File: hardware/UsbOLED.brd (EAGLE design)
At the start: 12.2 x 41.6 mm, 23 parts, among them U1 ATMEGA328P-MU-QFN32, X1 USBPCB

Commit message: urther refine
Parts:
- removed JP1: (no value), adafruit:1X06
- added H1: 1X6, headers(.1in):1X6
- R1: value 560kΩ -> 330kΩ
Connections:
- removed net N$10: C6.2, LCD1.5
- net +3V3: now also C6.2, H1.5, LCD1.5; no longer JP1.5
- net GND: now also H1.6; no longer JP1.6
- net MISO: now also H1.2; no longer JP1.2
- net MOSI: now also H1.1; no longer JP1.1
- net RST: now also H1.4; no longer JP1.4
- net SCK: now also H1.3; no longer JP1.3
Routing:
- net +3V3: track 61.4 -> 86.6 mm, vias 2 -> 4
- net N$10: track 18.2 -> 0.00 mm, vias 2 -> 0

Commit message: Improve routing, add version
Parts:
- removed C4: 10uF, rcl:C0603
- removed C6, C7: 1uF, rcl:C0603
- removed D3: (no value), diode:SOD523
- moved LOGO1 32.1 mm to (6.22, 4.57), flipped to the bottom
- moved D1 0.28 mm to (0.51, 11.2)
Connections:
- removed net N$11: C4.2, LCD1.14
- removed net N$9: C7.2, LCD1.8
- new net VCC: LCD1.14
- net +3V3: now also LCD1.8; no longer C6.2
- net +5V: no longer D3.C
- net GND: no longer C4.1, C6.1, C7.1
- net OLED_RESET: no longer D3.A
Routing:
- net D+: track 37.4 -> 18.2 mm
- net +5V: track 25.4 -> 9.63 mm, vias 2 -> 1
- net +3V3: track 86.6 -> 71.3 mm, vias 4 -> 5
- net SCK: track 14.1 -> 26.4 mm
- net N$9: track 9.04 -> 0.00 mm
- net OLED_RESET: track 15.5 -> 23.4 mm, vias 2 -> 0
- net GND: track 96.6 -> 92.1 mm
- net N$11: track 4.32 -> 0.00 mm
- net N$3: track 6.91 -> 10.5 mm, vias 0 -> 2
- net SDA: track 23.5 -> 26.4 mm, vias 3 -> 5
- net N$1: track 6.02 -> 8.57 mm, vias 0 -> 2
- net MISO: track 18.7 -> 21.2 mm
- net RST: track 12.2 -> 11.2 mm
- net D-: track 11.6 -> 12.1 mm
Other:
- board text added: "08.2018"
- board text added: "Mihai Galos"
- board text added: "UsbOLED v1.0.0"

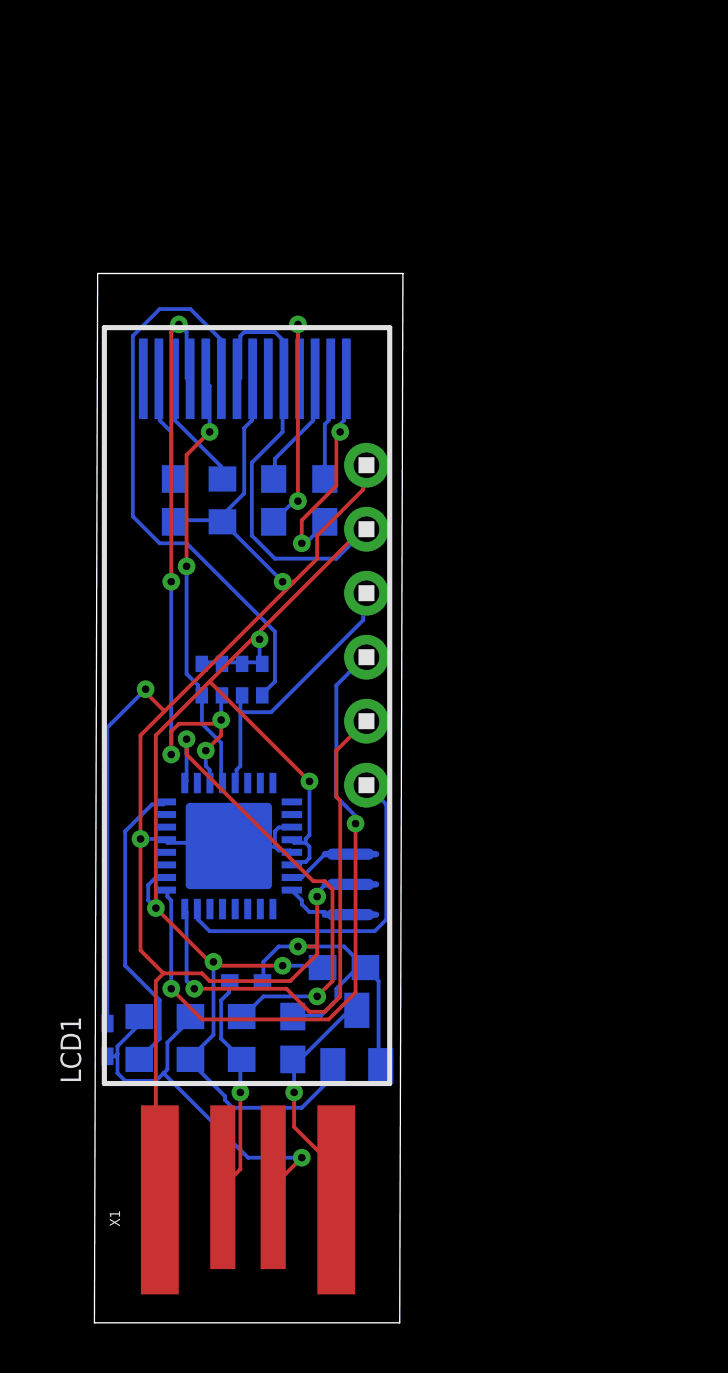
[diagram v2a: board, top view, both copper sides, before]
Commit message: Add pushbuttons A,B
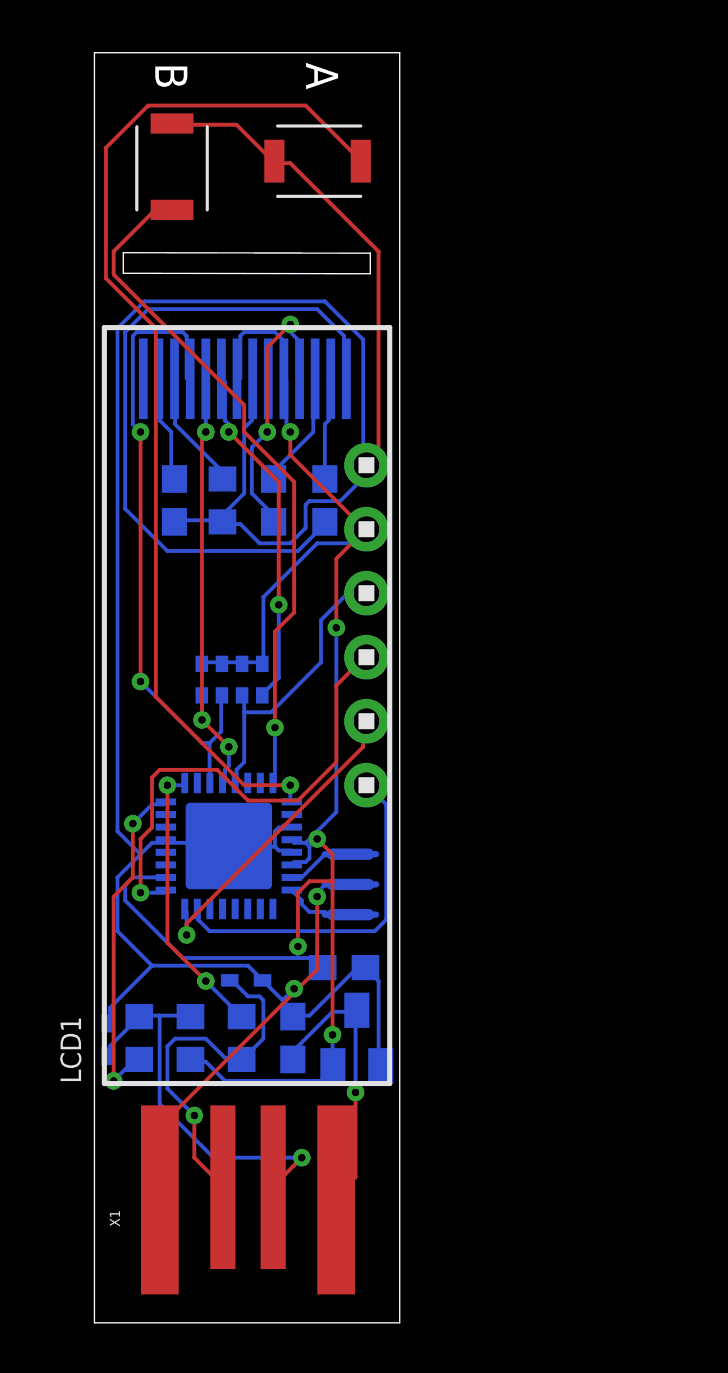
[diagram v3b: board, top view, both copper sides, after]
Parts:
- added U$1, U$3: PUSHBUTTON_4X2.5, pusbbutton_4x2_5:PUSHBUTTON_4X2.5
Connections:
- removed net PUSH: U1.1
- removed net RIRQ: U1.32
- new net PUSHA: U$1.P$1, U1.1
- new net PUSHB: U$3.P$1, U1.32
- net GND: now also U$1.P$2, U$3.P$2
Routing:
- net PUSHA: track 0.00 -> 41.8 mm, vias 0 -> 1
- net PUSHB: track 0.00 -> 27.5 mm, vias 0 -> 1
- net GND: track 92.1 -> 119.3 mm, vias 5 -> 2
- net N$1: track 8.57 -> 27.4 mm, vias 2 -> 0
- net OLED_RESET: track 23.4 -> 13.8 mm, vias 0 -> 2
- net MISO: track 21.2 -> 12.5 mm
- net SCK: track 26.4 -> 19.1 mm, vias 2 -> 1
- net D+: track 18.2 -> 11.1 mm
- net USB_D+: track 8.98 -> 14.3 mm
- net +5V: track 9.63 -> 11.3 mm
- net D-: track 12.1 -> 13.6 mm, vias 0 -> 2
- net +3V3: track 71.3 -> 69.9 mm
- net SDA: track 26.4 -> 25.4 mm, vias 5 -> 2
- net N$3: track 10.5 -> 11.2 mm
- net SCL: track 17.1 -> 17.6 mm, vias 2 -> 3
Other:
- board size 12.2 x 41.6 mm -> 12.1 x 50.4 mm
- board text added: "A"
- board text added: "B"

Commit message: Improve GND
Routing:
- net GND: vias 2 -> 22
- added copper zone on layer 1, net GND
- added copper zone on layer 16, net GND
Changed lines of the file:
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@@
 <setting verticaltext="up"/>
 </settings>
-<grid distance="0.00001" unitdist="mm" unit="mm" style="lines" multiple="1" display="no" altdistance="0.025" altunitdist="inch" altunit="inch"/>
+<grid distance="0.05" unitdist="mm" unit="mm" style="lines" multiple="1" display="no" altdistance="0.025" altunitdist="inch" altunit="inch"/>
 <layers>
 <layer number="1" name="Top" color="4" fill="1" visible="yes" active="yes"/>
@@
 <wire x1="1.14585" y1="42.47105" x2="1.14585" y2="41.655340625" width="0.0001" layer="20"/>
 <text x="8.39958125" y="50.01691875" size="1.27" layer="20" rot="SR270">A</text>
-<text x="2.41631875" y="50.01691875" size="1.27" layer="20" rot="SR270">B</text>
+<text x="2.31631875" y="49.91691875" size="1.27" layer="20" rot="SR270">B</text>
 </plain>
 <attributes>
@@
 <via x="8.8392" y="16.9164" extent="1-16" drill="0.3"/>
 <via x="7.9248" y="13.2588" extent="1-16" drill="0.3"/>
+<via x="8.687971875" y="23.06558125" extent="1-16" drill="0.3"/>
+<via x="2.459684375" y="22.763603125" extent="1-16" drill="0.3"/>
+<via x="1.783634375" y="23.914003125" extent="1-16" drill="0.3"/>
+<via x="3.178884375" y="25.65399375" extent="1-16" drill="0.3"/>
+<via x="3.365875" y="29.00454375" extent="1-16" drill="0.3"/>
+<via x="5.667325" y="29.57974375" extent="1-16" drill="0.3"/>
+<via x="8.7886625" y="29.36404375" extent="1-16" drill="0.3"/>
+<via x="6.0131125" y="43.347184375" extent="1-16" drill="0.3"/>
+<via x="5.3916625" y="49.196984375" extent="1-16" drill="0.3"/>
+<via x="0.79984375" y="48.454975" extent="1-16" drill="0.3"/>
+<via x="10.82934375" y="48.489484375" extent="1-16" drill="0.3"/>
+<via x="11.2609125" y="43.95115625" extent="1-16" drill="0.3"/>
+<via x="10.245171875" y="40.729934375" extent="1-16" drill="0.3"/>
+<polygon width="0.1" layer="1">
+<vertex x="0.25" y="9"/>
+<vertex x="12.25" y="9"/>
+<vertex x="12" y="50.5"/>
+<vertex x="0" y="50.5"/>
+</polygon>
+<polygon width="0.1524" layer="16">
+<vertex x="0" y="9"/>
+<vertex x="12" y="9"/>
+<vertex x="12" y="50.5"/>
+<vertex x="0" y="50.5"/>
+</polygon>
+<via x="1.459684375" y="14.263603125" extent="1-16" drill="0.3"/>
+<via x="2.709684375" y="13.513603125" extent="1-16" drill="0.3"/>
+<via x="1.033634375" y="28.414003125" extent="1-16" drill="0.3"/>
+<via x="1.033634375" y="30.914003125" extent="1-16" drill="0.3"/>
+<via x="10.995171875" y="37.479934375" extent="1-16" drill="0.3"/>
+<via x="5.337971875" y="18.91558125" extent="1-16" drill="0.3"/>
+<via x="5.5131125" y="45.897184375" extent="1-16" drill="0.3"/>
 </signal>
 <signal name="SDA">
